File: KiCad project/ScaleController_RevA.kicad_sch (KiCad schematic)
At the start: 13 parts, among them J1 TYPE-C-31-M-12, U2 LM1117MPX-3.3_NOPB

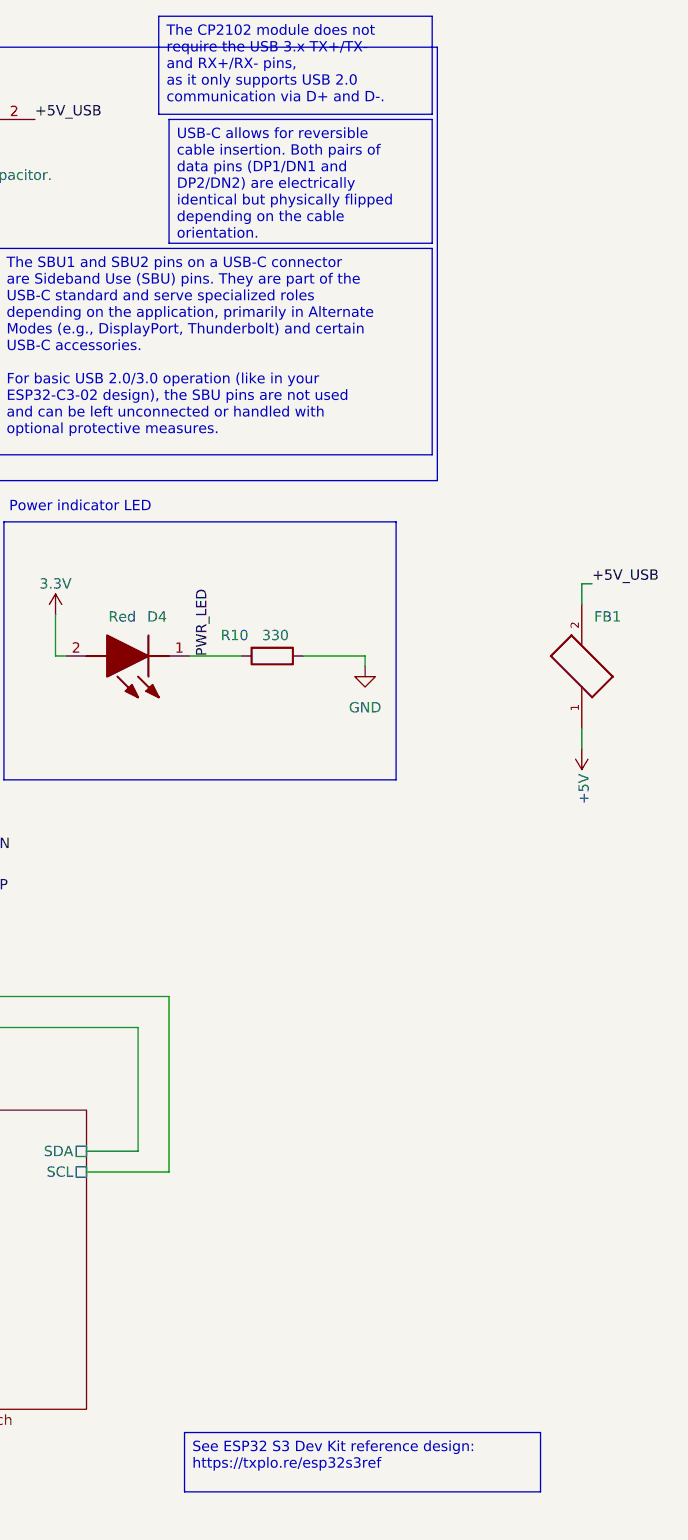
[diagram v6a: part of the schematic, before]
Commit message: Schematic: title blocks (Scale Controller, rev A, 2026-09-18, per-sheet comments); replace stale CP2102 and ESP32-S3 notes
Co-Authored-By: Claude Fable 5.1 <noreply@anthropic.com>
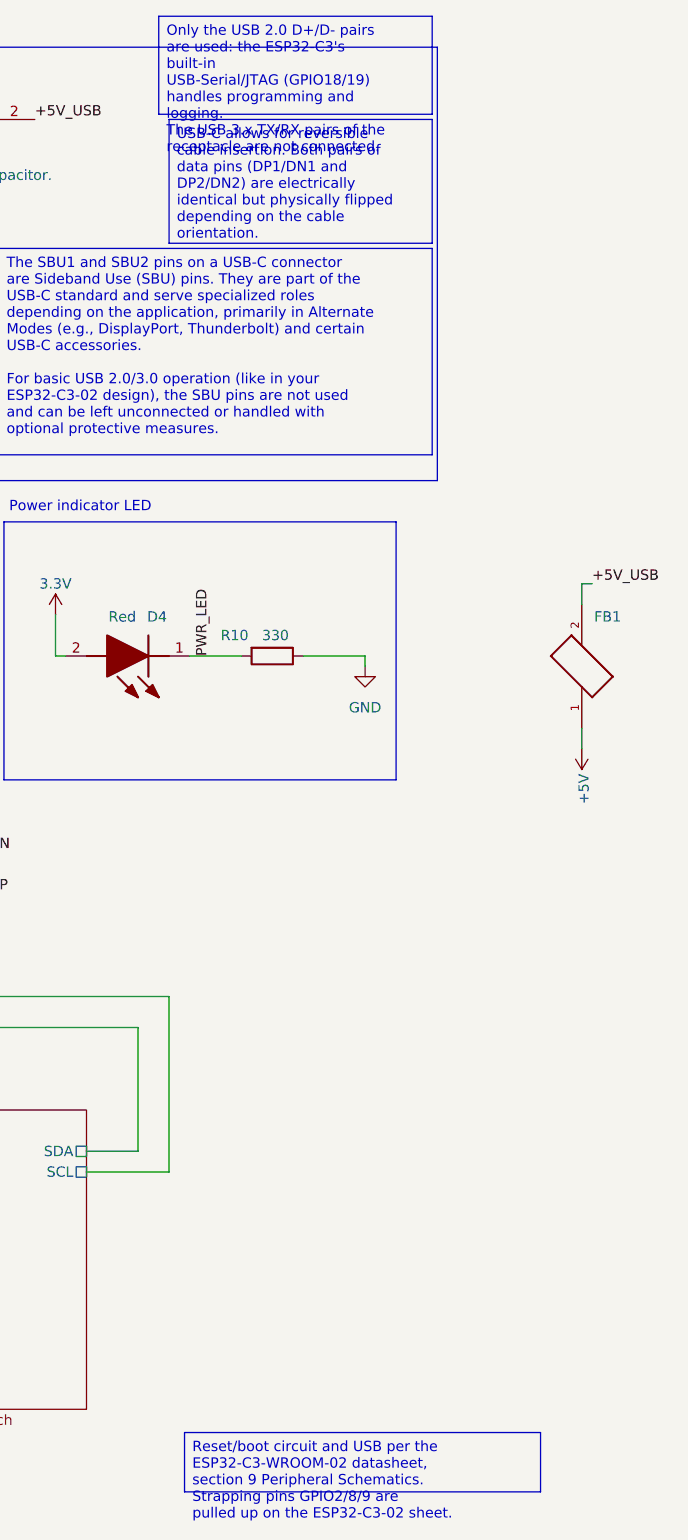
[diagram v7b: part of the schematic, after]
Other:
- company: (none) -> Steve Maegley
- title: ESP32 sensor board -> Scale Controller
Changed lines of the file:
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@@
 	(paper "A4")
 	(title_block
-		(title "ESP32 sensor board")
-		(date "2024-11-22")
-		(rev "1")
-		(comment 1 "OLED Header")
+		(title "Scale Controller")
+		(date "2026-09-18")
+		(rev "A")
+		(company "Steve Maegley")
+		(comment 1 "Root: USB-C, power, sheet index")
 	)
 	(rectangle
@@
 		)
 	)
-	(text_box "The CP2102 module does not require the USB 3.x TX+/TX- and RX+/RX- pins, \nas it only supports USB 2.0 communication via D+ and D-."
+	(text_box "Only the USB 2.0 D+/D- pairs are used: the ESP32-C3's built-in\nUSB-Serial/JTAG (GPIO18/19) handles programming and logging.\nThe USB 3.x TX/RX pairs of the receptacle are not connected."
 		(exclude_from_sim no)
 		(at 125.73 13.97 0)
@@
 		)
 	)
-	(text_box "See ESP32 S3 Dev Kit reference design:\nhttps://txplo.re/esp32s3ref"
+	(text_box "Reset/boot circuit and USB per the ESP32-C3-WROOM-02 datasheet,\nsection 9 Peripheral Schematics. Strapping pins GPIO2/8/9 are\npulled up on the ESP32-C3-02 sheet."
 		(exclude_from_sim no)
 		(at 128.905 188.2775 0)
